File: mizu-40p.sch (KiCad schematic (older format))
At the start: 128 parts, among them SW1 SW_Push, U1 ATmega32U4-AU, Y1 16MHz

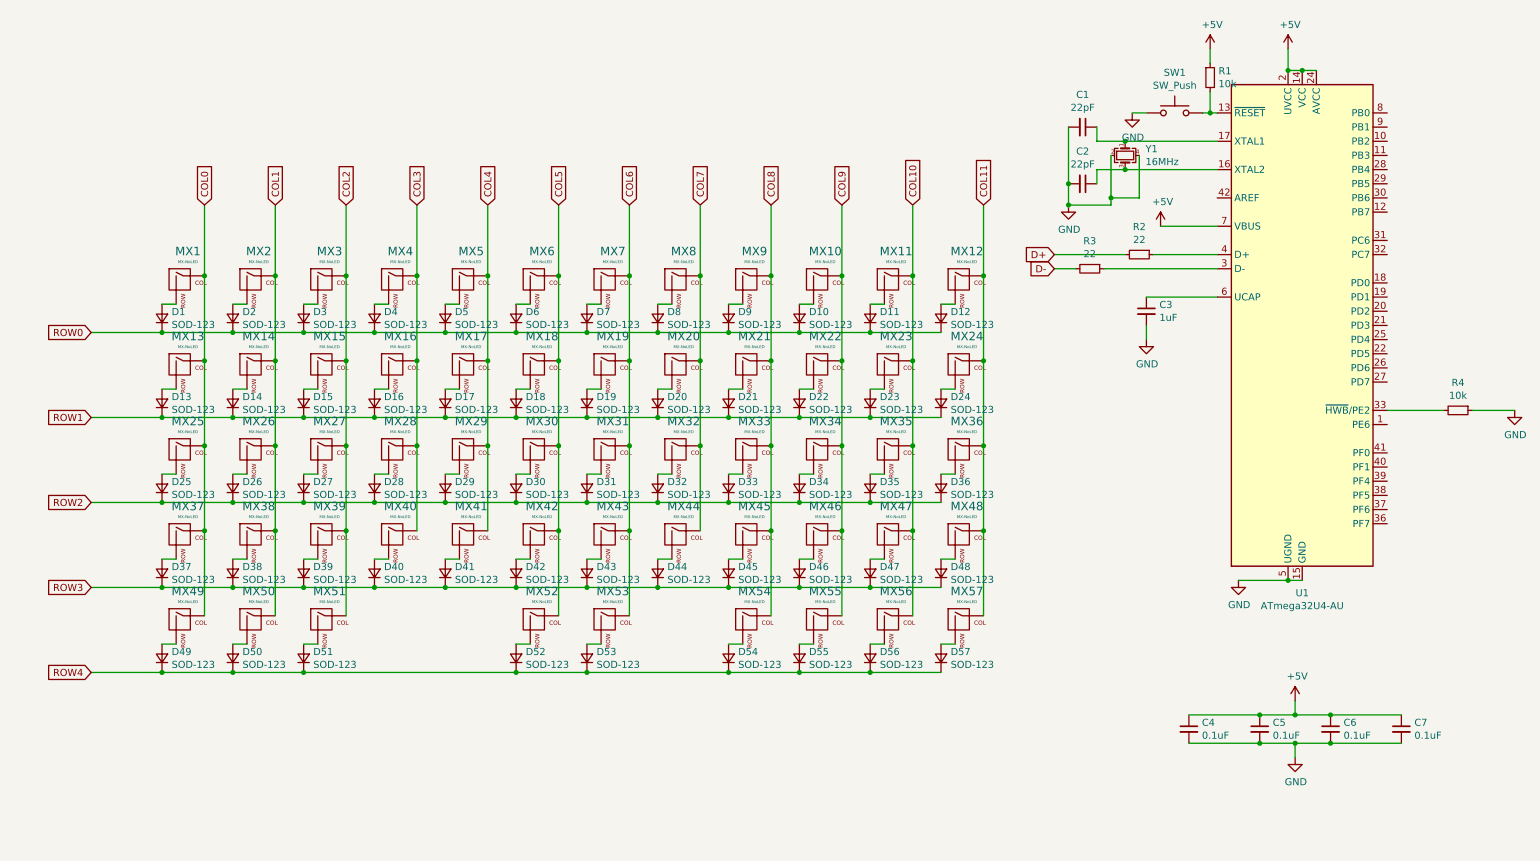
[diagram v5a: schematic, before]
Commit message: Change switch matrix
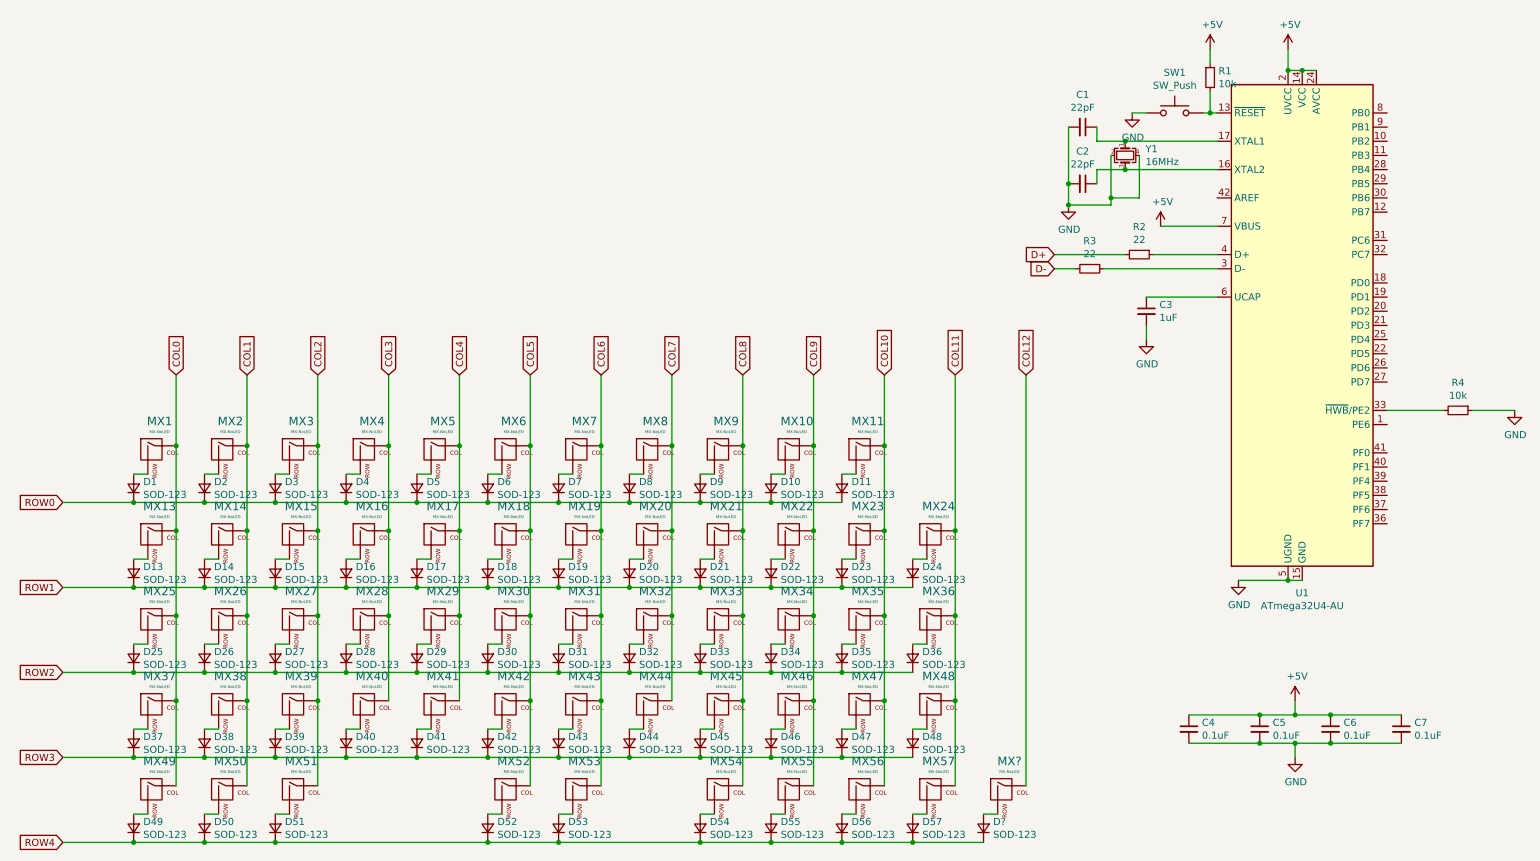
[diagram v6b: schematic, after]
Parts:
- removed D12: SOD-123, Diode_SMD:D_SOD-123, symbol Device:D_Small
- removed MX12: MX-NoLED, MX_Alps_Hybrid:MX-1U-NoLED, symbol MX_Alps_Hybrid:MX-NoLED
- added D?: SOD-123, Diode_SMD:D_SOD-123, symbol Device:D_Small
- added MX?: MX-NoLED, MX_Alps_Hybrid:MX-1U-NoLED, symbol MX_Alps_Hybrid:MX-NoLED
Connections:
- net ROW4: now also D?.1 (K)
- new net: D?.2 (A), MX?.2 (ROW)
- new net COL12: MX?.1 (COL)
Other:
- moved on the sheet: D1, D10, D11, D13, D14, D15, D16, D17, D18, D19, D2, D20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

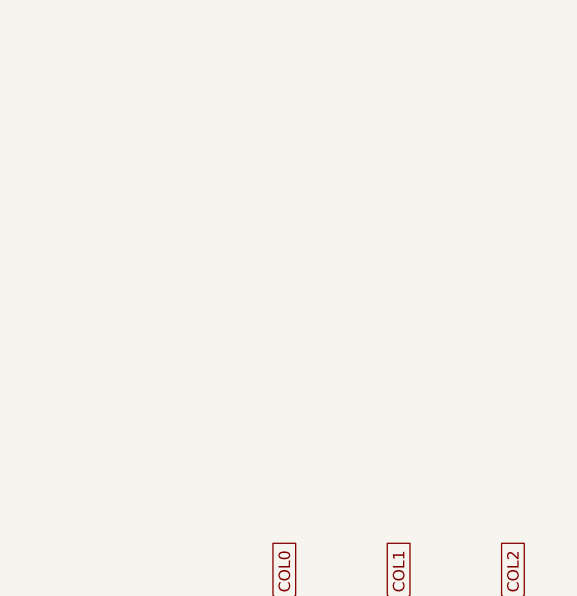
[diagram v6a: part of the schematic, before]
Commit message: Add Connector_USB_C_Receptable_USB2.0
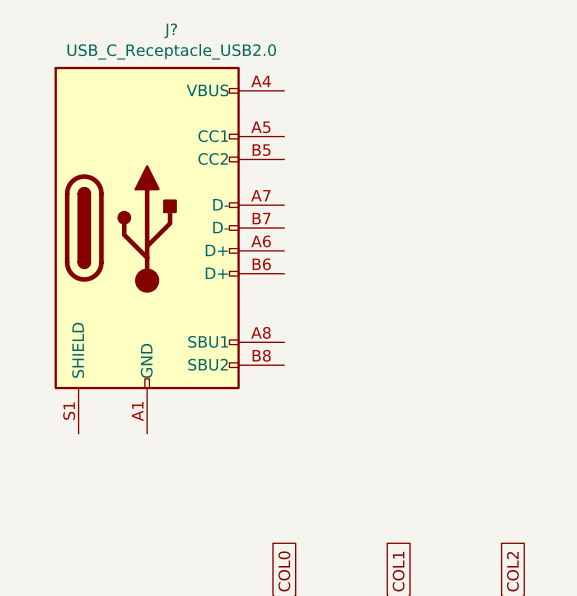
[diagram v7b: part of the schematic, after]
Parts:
- added J?: USB_C_Receptacle_USB2.0, symbol Connector:USB_C_Receptacle_USB2.0
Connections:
- new net: J?.A1 (GND), J?.A12 (GND), J?.B1 (GND), J?.B12 (GND)
- new net: J?.A4 (VBUS), J?.A9 (VBUS), J?.B4 (VBUS), J?.B9 (VBUS)
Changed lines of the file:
@@
 	7600 3100 7600 6000
 Connection ~ 6800 6400
+$Comp
+L Connector:USB_C_Receptacle_USB2.0 J?
+U 1 1 628B6CDF
+P 1000 1450
+F 0 "J?" H 1107 2317 50  0000 C CNN
+F 1 "USB_C_Receptacle_USB2.0" H 1107 2226 50  0000 C CNN
+F 2 "" H 1150 1450 50  0001 C CNN
+F 3 "https://www.usb.org/sites/default/files/documents/usb_type-c.zip" H 1150 1450 50  0001 C CNN
+	1    1000 1450
+	1    0    0    -1
+$EndComp
 $EndSCHEMATC
